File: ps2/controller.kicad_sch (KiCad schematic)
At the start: 14 parts, among them Q5 BC547B, Q6 BC547B, U1 74HC74, U7 74HC00, U8 74HC14

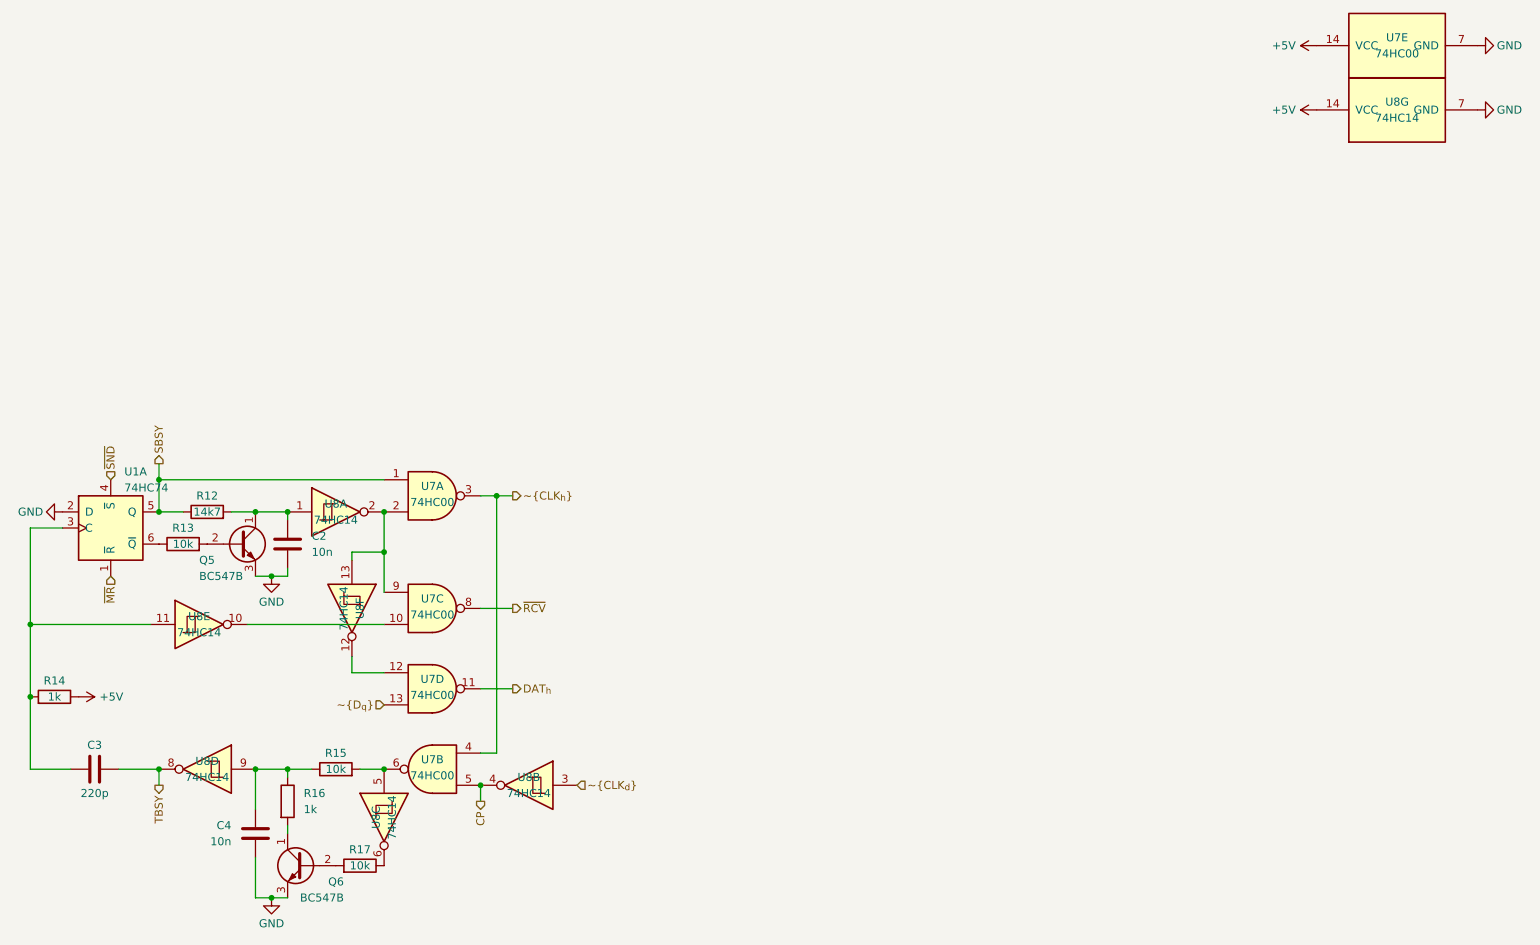
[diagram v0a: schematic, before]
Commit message: [ps2]:	made pcb design of the new latest schematic
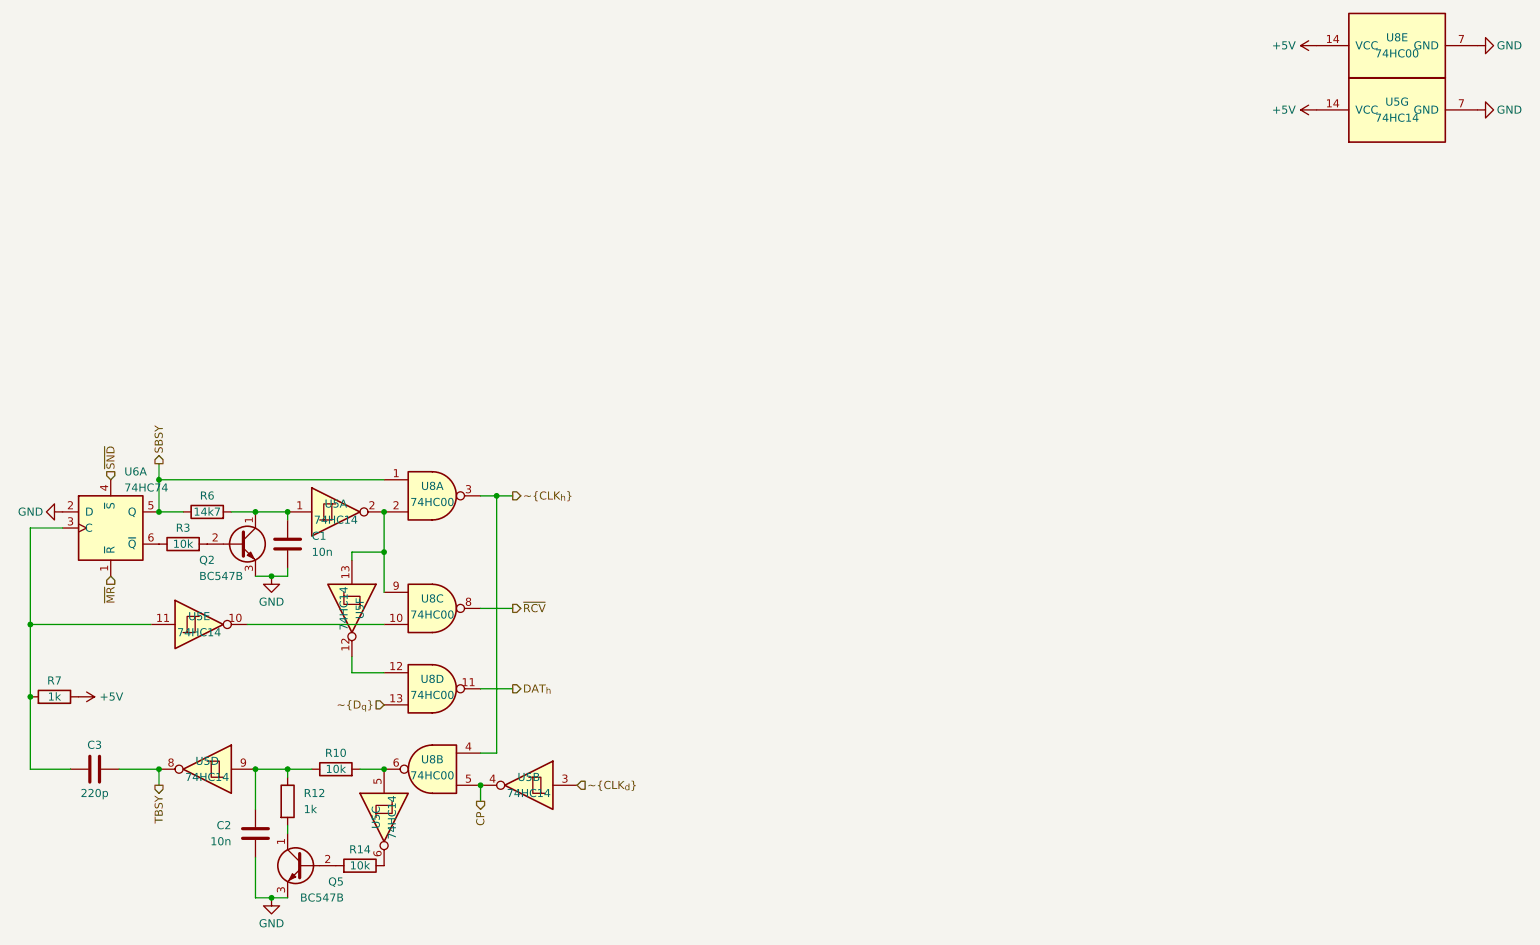
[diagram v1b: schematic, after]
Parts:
- renumbered C2 to C1, C4 to C2, Q5 to Q2, Q6 to Q5, R15 to R10, R16 to R12, R17 to R14, R13 to R3, R12 to R6, R14 to R7, U8 to U5, U1 to U6, U7 to U8
